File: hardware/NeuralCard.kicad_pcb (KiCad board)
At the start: 2 copper layers, 85.6 x 54 mm, 66 parts, among them J1 ProgPads, J2 TYPE-C-31-M-12, Q1 AO3401A, SW1 SW-SMD_4P-L5.1-W5.1-P3.70-LS6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, SW2 SW-SMD_4P-L5.1-W5.1-P3.70-LS6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, SW3 SW_SPDT_Shouhan_MSK12C02, U1 WIRELM-SMD_ESP32-S3-WROOM-1, U2 LGA-14_L3.0-W2.5-P0.50-TL, U3 ME6211C33M5G-N, U4 SO-8_L4.9-W3.9-P1.27-LS5.9-BL, U5 USBLC6-2SC6

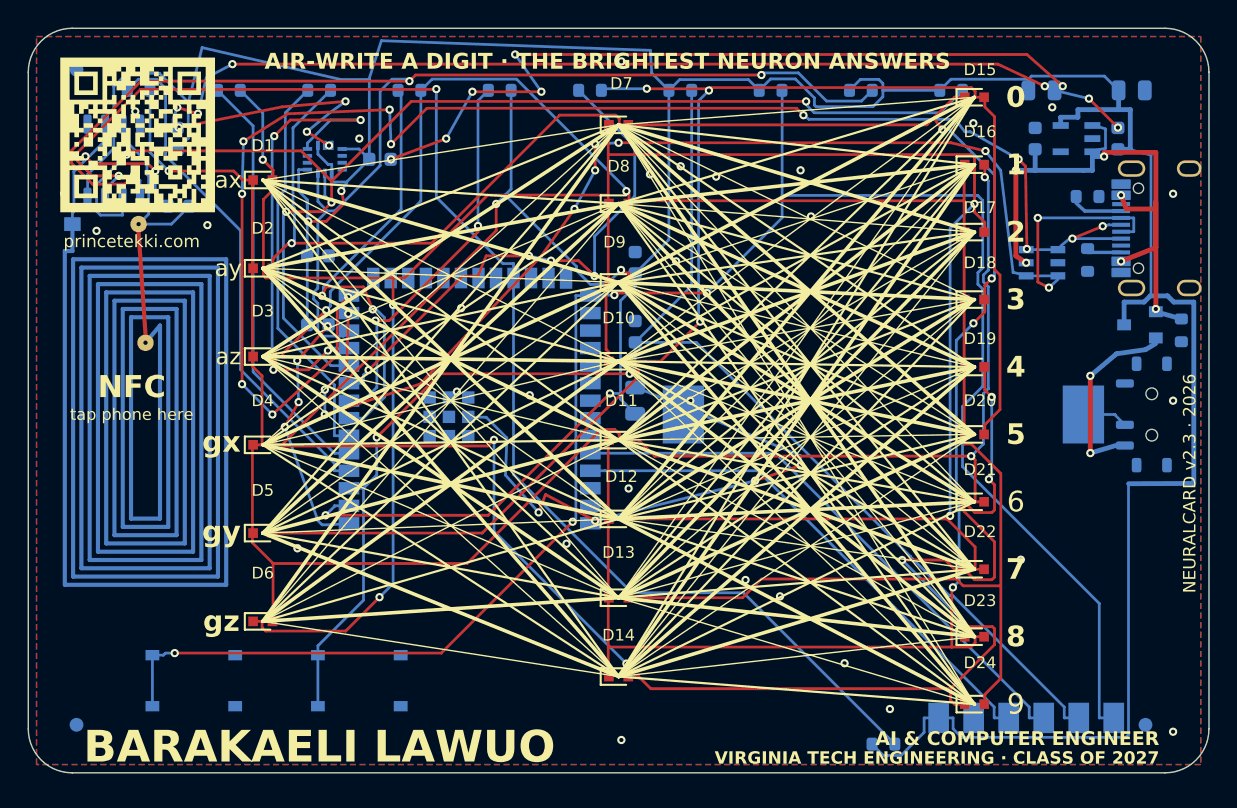
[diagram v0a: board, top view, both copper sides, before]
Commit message: fix corners and decoupling
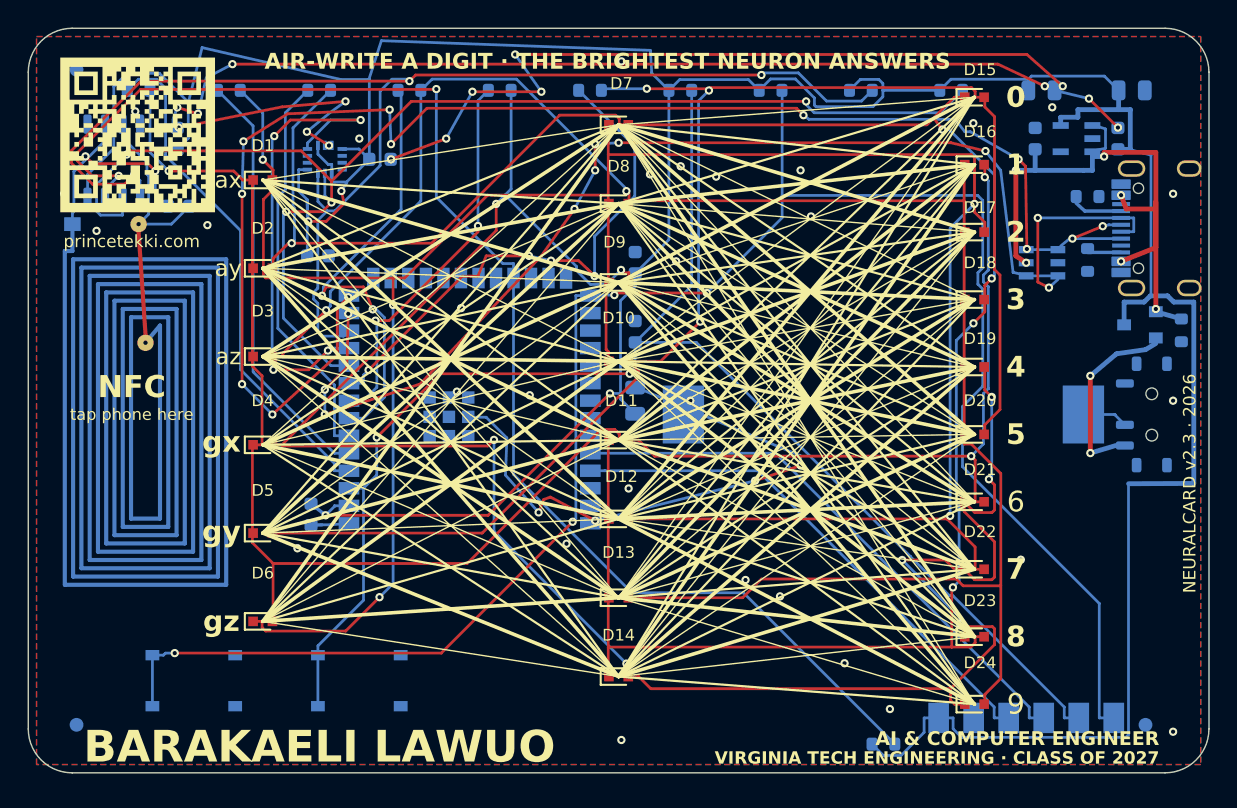
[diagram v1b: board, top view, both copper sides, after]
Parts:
- moved C2 13.8 mm to (20.5, 35.2), turned to -90 degrees
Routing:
- net GND: track 211.9 -> 196.3 mm, vias 54 -> 50
- net +3V3: track 275.7 -> 271.6 mm
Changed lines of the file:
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@@
 	(footprint "C_0603_1608Metric"
 		(layer "B.Cu")
-		(at 21 21.5)
+		(at 20.5 35.25 -90)
 		(descr "Capacitor SMD 0603 (1608 Metric), square (rectangular) end terminal, IPC-7351 nominal, (Body size source: IPC-SM-782 page 76, https://www.pcb-3d.com/wordpress/wp-content/uploads/ipc-sm-782a_amendment_1_and_2.pdf)")
 		(tags "capacitor")
 		(property "Reference" "C2"
-			(at 0 1.43 180)
+			(at 0 1.43 90)
 			(layer "B.SilkS")
 			(effects
@@
 		)
 		(property "Value" "C_0603_1608Metric"
-			(at 0 -1.43 180)
+			(at 0 -1.43 90)
 			(layer "B.Fab")
 			(effects
@@
 		)
 		(property "Datasheet" ""
-			(at 0 0 180)
+			(at 0 0 90)
 			(layer "B.Fab")
 			(hide yes)
@@
 		)
 		(property "Description" ""
-			(at 0 0 180)
+			(at 0 0 90)
 			(layer "B.Fab")
 			(hide yes)
@@
 		)
 		(property "KiLib_Generator" "SMD_2terminal_chip_molded"
-			(at 0 0 180)
+			(at 0 0 90)
 			(layer "B.SilkS")
 			(hide yes)
@@
 		(duplicate_pad_numbers_are_jumpers no)
 		(fp_line
-			(start -0.14058 -0.51)
-			(end 0.14058 -0.51)
+			(start -0.14058 0.51)
+			(end 0.14058 0.51)
 			(stroke
 				(width 0.12)
@@
 		)
 		(fp_line
-			(start -0.14058 0.51)
-			(end 0.14058 0.51)
+			(start -0.14058 -0.51)
+			(end 0.14058 -0.51)
 			(stroke
 				(width 0.12)
@@
 		)
 		(fp_text user "${REFERENCE}"
-			(at 0 0 180)
+			(at 0 0 90)
 			(layer "B.Fab")
 			(effects
@@
 		)
 		(pad "1" smd roundrect
-			(at -0.775 0)
+			(at -0.775 0 270)
 			(size 0.9 0.95)
 			(layers "B.Cu" "B.Mask" "B.Paste")
@@
 		)
 		(pad "2" smd roundrect
-			(at 0.775 0)
+			(at 0.775 0 270)
 			(size 0.9 0.95)
 			(layers "B.Cu" "B.Mask" "B.Paste")
@@
 	(segment
 		(start 44.2328 24.8258)
-		(end 43.55 24.143)
+		(end 43.788979 24.38198)
 		(width 0.2)
 		(layer "F.Cu")
@@
 	)
 	(segment
-		(start 45.8435 24.143)
-		(end 43.55 24.143)
+		(start 70.0518 17.4881)
+		(end 70.0517 17.4881)
 		(width 0.2)
 		(layer "F.Cu")
@@
 	)
 	(segment
-		(start 70.0518 17.4881)
-		(end 70.0517 17.4881)
+		(start 49.3484 4.3819)
+		(end 49.3484 4.5101)
 		(width 0.2)
 		(layer "F.Cu")
@@
 	)
 	(segment
-		(start 49.3484 4.3819)
-		(end 49.3484 4.5101)
+		(start 43.788979 24.38198)
+		(end 43.887968 24.143)
 		(width 0.2)
 		(layer "F.Cu")
@@
 		(net "CP6")
 	)
+	(segment
+		(start 43.887968 24.143)
+		(end 45.8435 24.143)
+		(width 0.2)
+		(layer "F.Cu")
+		(net "CP6")
+	)
 	(via
 		(at 48.7186 21.2679)
@@
 	)
 	(segment
-		(start 69.8624 39.9789)
-		(end 68.6069 39.9789)
+		(start 67.85 34.578595)
+		(end 68.023661 34.506661)
 		(width 0.2)
 		(layer "F.Cu")
@@
 	)
 	(segment
-		(start 67.85 34.333)
-		(end 67.85 35.0347)
+		(start 69.8624 39.9789)
+		(end 68.6069 39.9789)
 		(width 0.2)
 		(layer "F.Cu")
@@
 	)
 	(segment
+		(start 67.85 35.0347)
+		(end 67.85 34.578595)
+		(width 0.2)
+		(layer "F.Cu")
+		(net "CP5")
+	)
+	(segment
 		(start 18.3922 30.2)
 		(end 18.4517 30.2)
@@
 	)
 	(segment
-		(start 68.6281 35.1111)
-		(end 67.85 34.333)
-		(width 0.2)
-		(layer "F.Cu")
-		(net "CP5")
-	)
-	(segment
 		(start 43.55 46.2473)
 		(end 43.55 47)
@@
 	)
 	(segment
+		(start 68.023661 34.506661)
+		(end 68.6281 35.1111)
+		(width 0.2)
+		(layer "F.Cu")
+		(net "CP5")
+	)
+	(segment
 		(start 18.4767 30.2845)
 		(end 18.3922 30.2)
@@
 	)
 	(segment
-		(start 79.05 5.9)
-		(end 79.9 5.9)
-		(width 0.35)
+		(start 20.5 34.475)
+		(end 21.56 35.31)
+		(width 0.25)
 		(layer "B.Cu")
 		(net "+3V3")
 	)
 	(segment
-		(start 79.9 8.78)
-		(end 79.45 8.78)
+		(start 79.05 5.9)
+		(end 79.9 5.9)
 		(width 0.35)
 		(layer "B.Cu")
@@
 	)
 	(segment
-		(start 20.225 16.5)
-		(end 20.225 21.5)
-		(width 0.2)
-		(layer "B.Cu")
-		(net "+3V3")
-	)
-	(segment
 		(start 74.85 7.05)
 		(end 74.85 6.45)
@@
 	)
 	(segment
-		(start 21.7 21.6)
-		(end 19.5 24.1)
-		(width 0.2)
-		(layer "F.Cu")
-		(net "GND")
-	)
-	(segment
 		(start 32.2 4.6)
 		(end 37.2 4.6)
@@
 	)
 	(segment
-		(start 41.1 35.7)
-		(end 37.5 33.8)
+		(start 72.4 1.9)
+		(end 75 4.2)
 		(width 0.2)
 		(layer "F.Cu")
@@
 	)
 	(segment
-		(start 19.6 27.1)
-		(end 18.6 28.9)
+		(start 23 5.3)
+		(end 18.4 5.7)
 		(width 0.2)
 		(layer "F.Cu")
@@
 	)
 	(segment
-		(start 72.4 1.9)
-		(end 75 4.2)
+		(start 37.356408 34.173338)
+		(end 37 35.1)
 		(width 0.2)
 		(layer "F.Cu")
@@
 	)
 	(segment
-		(start 23 5.3)
-		(end 18.4 5.7)
+		(start 41.1 35.7)
+		(end 37.853753 33.986703)
 		(width 0.2)
 		(layer "F.Cu")
@@
 	)
 	(segment
-		(start 37.5 33.8)
-		(end 37 35.1)
+		(start 18.4 5.7)
+		(end 10.9 7.2)
 		(width 0.2)
 		(layer "F.Cu")
@@
 	)
 	(segment
-		(start 18.4 5.7)
-		(end 10.9 7.2)
+		(start 37.853753 33.986703)
+		(end 37.356408 34.173338)
 		(width 0.2)
 		(layer "F.Cu")
@@
 	)
 	(via
-		(at 19.6 27.1)
-		(size 0.6)
-		(drill 0.3)
-		(layers "F.Cu" "B.Cu")
-		(net "GND")
-	)
-	(via
 		(at 52.7 32.8)
 		(size 0.6)
@@
 	)
 	(via
-		(at 19.5 24.1)
-		(size 0.6)
-		(drill 0.3)
-		(layers "F.Cu" "B.Cu")
-		(net "GND")
-	)
-	(via
 		(at 30.3 8)
 		(size 0.6)
@@
 	)
 	(via
-		(at 18.6 28.9)
-		(size 0.6)
-		(drill 0.3)
-		(layers "F.Cu" "B.Cu")
-		(net "GND")
-	)
-	(via
 		(at 36.355615 26.605528)
 		(size 0.6)
@@
 	)
 	(via
-		(at 21.7 21.6)
-		(size 0.6)
-		(drill 0.3)
-		(layers "F.Cu" "B.Cu")
-		(net "GND")
-	)
-	(via
 		(at 39.025 37.369)
 		(size 0.6)
@@
 	)
 	(segment
-		(start 21.8 21.5)
-		(end 21.7 21.6)
-		(width 0.2)
-		(layer "B.Cu")
-		(net "GND")
-	)
-	(segment
 		(start 37 35.1)
 		(end 34.6 32.4)
@@
 	)
 	(segment
-		(start 18.6 28.9)
-		(end 21 35.7)
-		(width 0.2)
+		(start 20.5 36.025)
+		(end 21.3 36)
+		(width 0.25)
 		(layer "B.Cu")
 		(net "GND")
@@
 	)
 	(segment
-		(start 21 35.7)
-		(end 21.3 36)
-		(width 0.2)
-		(layer "B.Cu")
-		(net "GND")
-	)
-	(segment
 		(start 21.9 36)
 		(end 23.2 35.9)
@@
 	)
 	(segment
-		(start 19.5 24.1)
-		(end 19.6 27.1)
-		(width 0.2)
-		(layer "B.Cu")
-		(net "GND")
-	)
-	(segment
 		(start 44 26)
 		(end 56 31)
@@
 	)
 	(segment
-		(start 8.604 9.7017)
-		(end 8.604 10.5927)
+		(start 10.375 14.2)
+		(end 8.361331 14.2)
 		(width 0.2)
 		(layer "B.Cu")
@@
 	)
 	(segment
-		(start 8.604 10.593)
-		(end 8.73 10.719)
+		(start 8.2555 13.9445)
+		(end 8.73 13.47)
 		(width 0.2)
 		(layer "B.Cu")
@@
 	)
 	(segment
-		(start 10.375 14.2)
-		(end 8 14.2)
+		(start 8.604 9.7017)
+		(end 8.604 10.5927)
+		(width 0.2)
+		(layer "B.Cu")
+		(net "NFC_ANT_B")
+	)
+	(segment
+		(start 8.604 10.593)
+		(end 8.73 10.719)
 		(width 0.2)
 		(layer "B.Cu")
@@
 	)
 	(segment
-		(start 8.73 13.47)
-		(end 8 14.2)
+		(start 8.361331 14.2)
+		(end 8.2555 13.9445)
 		(width 0.2)
 		(layer "B.Cu")

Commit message: bump to v2.3.1
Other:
- board text added: "NEURALCARD v2.3.1 · 2026"
- board text added: "NeuralCard v2.3.1 · princetekki.com"
- board text removed: "NEURALCARD v2.3 · 2026"
- board text removed: "NeuralCard v2.3 · princetekki.com"
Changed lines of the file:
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@@
 		(title "NeuralCard")
 		(date "2026-08-07")
-		(rev "v2.3")
+		(rev "v2.3.1")
 	)
 	(layers
@@
 		)
 	)
-	(gr_text "NEURALCARD v2.3 · 2026"
+	(gr_text "NEURALCARD v2.3.1 · 2026"
 		(at 84.2 33 90)
 		(layer "F.SilkS")
@@
 		)
 	)
-	(gr_text "NeuralCard v2.3 · princetekki.com"
+	(gr_text "NeuralCard v2.3.1 · princetekki.com"
 		(at 65.5 42.5 0)
 		(layer "B.SilkS")
